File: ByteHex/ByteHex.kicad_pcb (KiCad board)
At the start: 2 copper layers, 25.4 x 20.3 mm, 18 parts, among them J1 Conn_01x08_Pin, J2 Conn_01x01_Socket, J3 Conn_01x01_Socket, J4 Conn_01x01_Socket, J5 ISP, SW4 SW_DIP_x04, U1 ATmega328PB-M

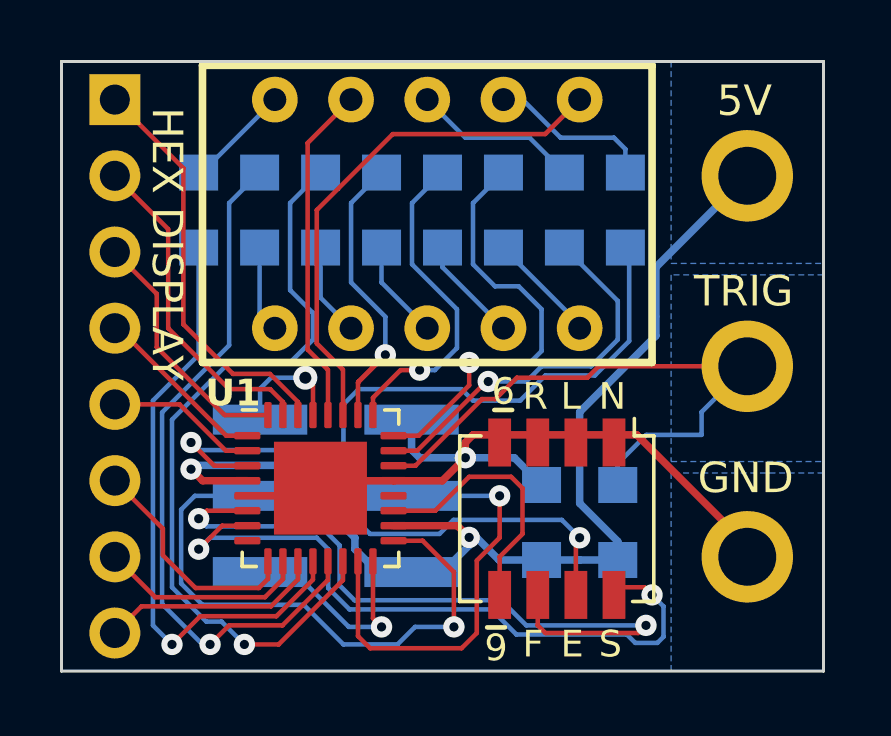
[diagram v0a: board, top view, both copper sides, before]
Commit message: Add pullup resistors to ClockGen and ByteHex
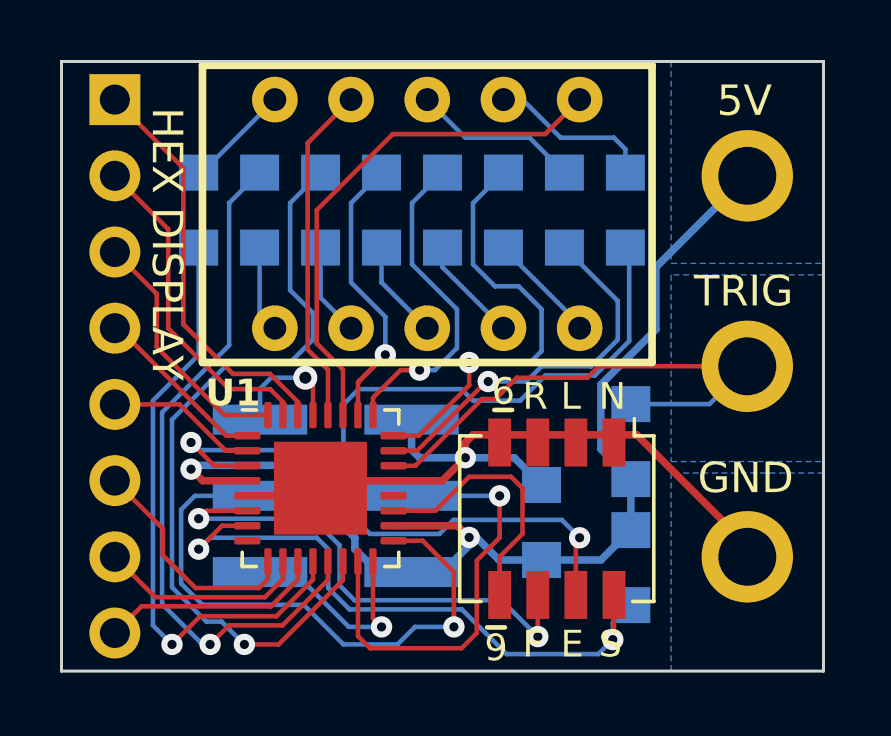
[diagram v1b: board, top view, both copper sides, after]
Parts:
- added R10: 4.7K, Passive:RESC2012X55, B.Cu at (144.2, 117.2)
- moved R1 2.73 mm to (144.2, 113.0)
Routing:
- net Net-(U1-PE1): track 24.0 -> 17.1 mm
- net Net-(J4-Pin_1): track 20.5 -> 18.1 mm
- net Net-(U1-XTAL1/PB6): track 22.8 -> 21.6 mm
- net VCC: track 37.9 -> 37.3 mm
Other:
- board text added: "This work is licensed under the Creative Commons Attribute-ShareAlike 4.0 International License. To view a copy of this license, visit http://creativecommons.org/license/by-sa/4.0/ or send a letter to Creative Commons, PO Box 1866, Mountain View, CA 94042, USA."
